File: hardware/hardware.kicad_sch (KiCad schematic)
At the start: 1 part, among them U1 ESP32-S3

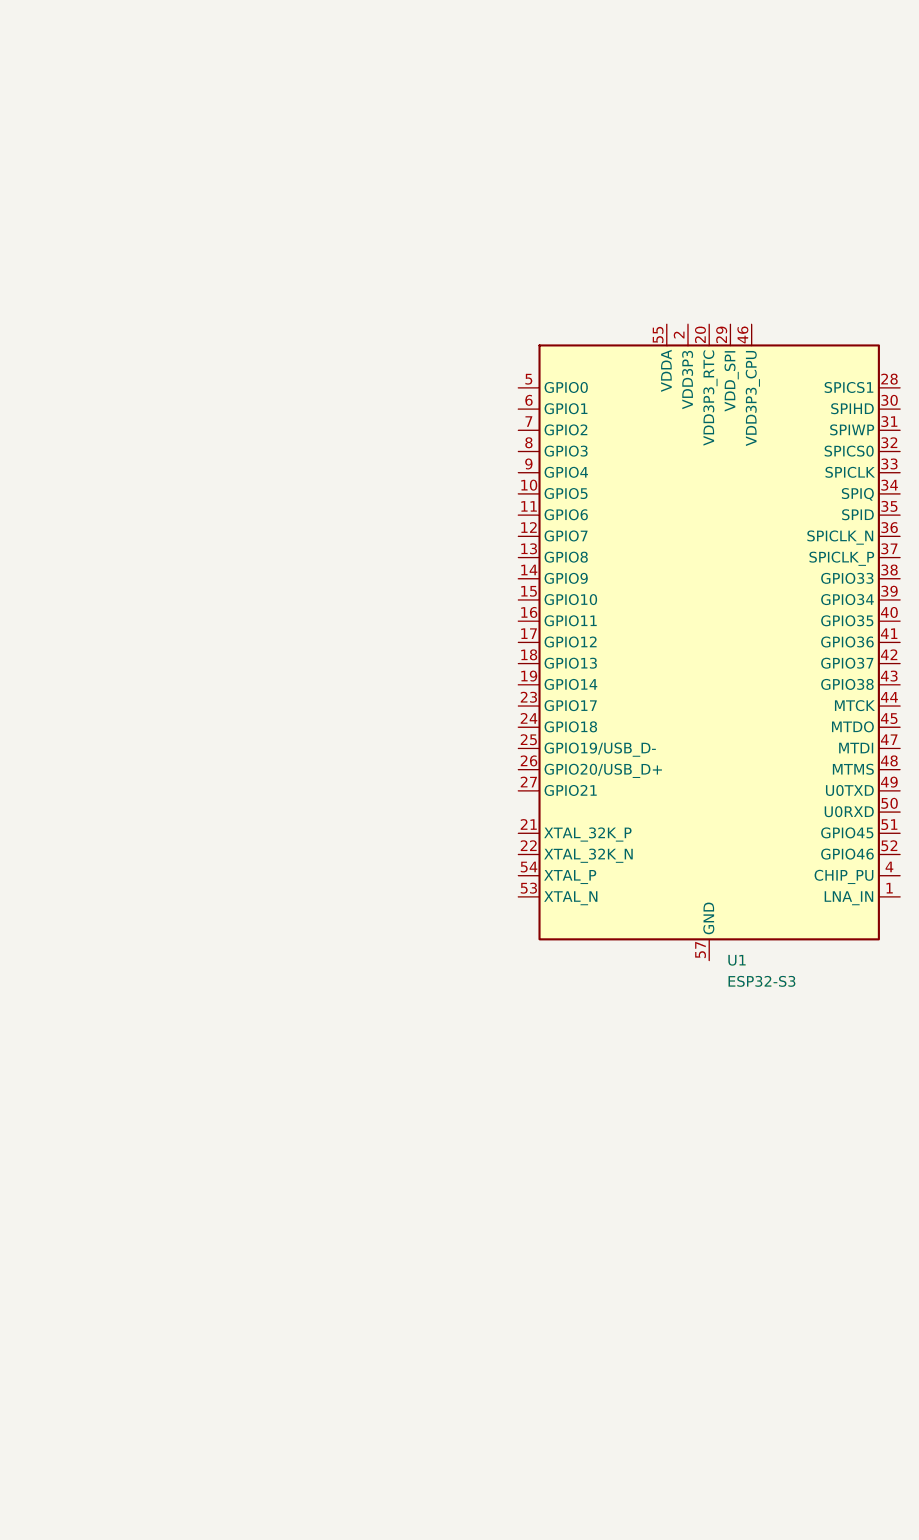
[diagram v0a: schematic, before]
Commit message: Adding usbc port
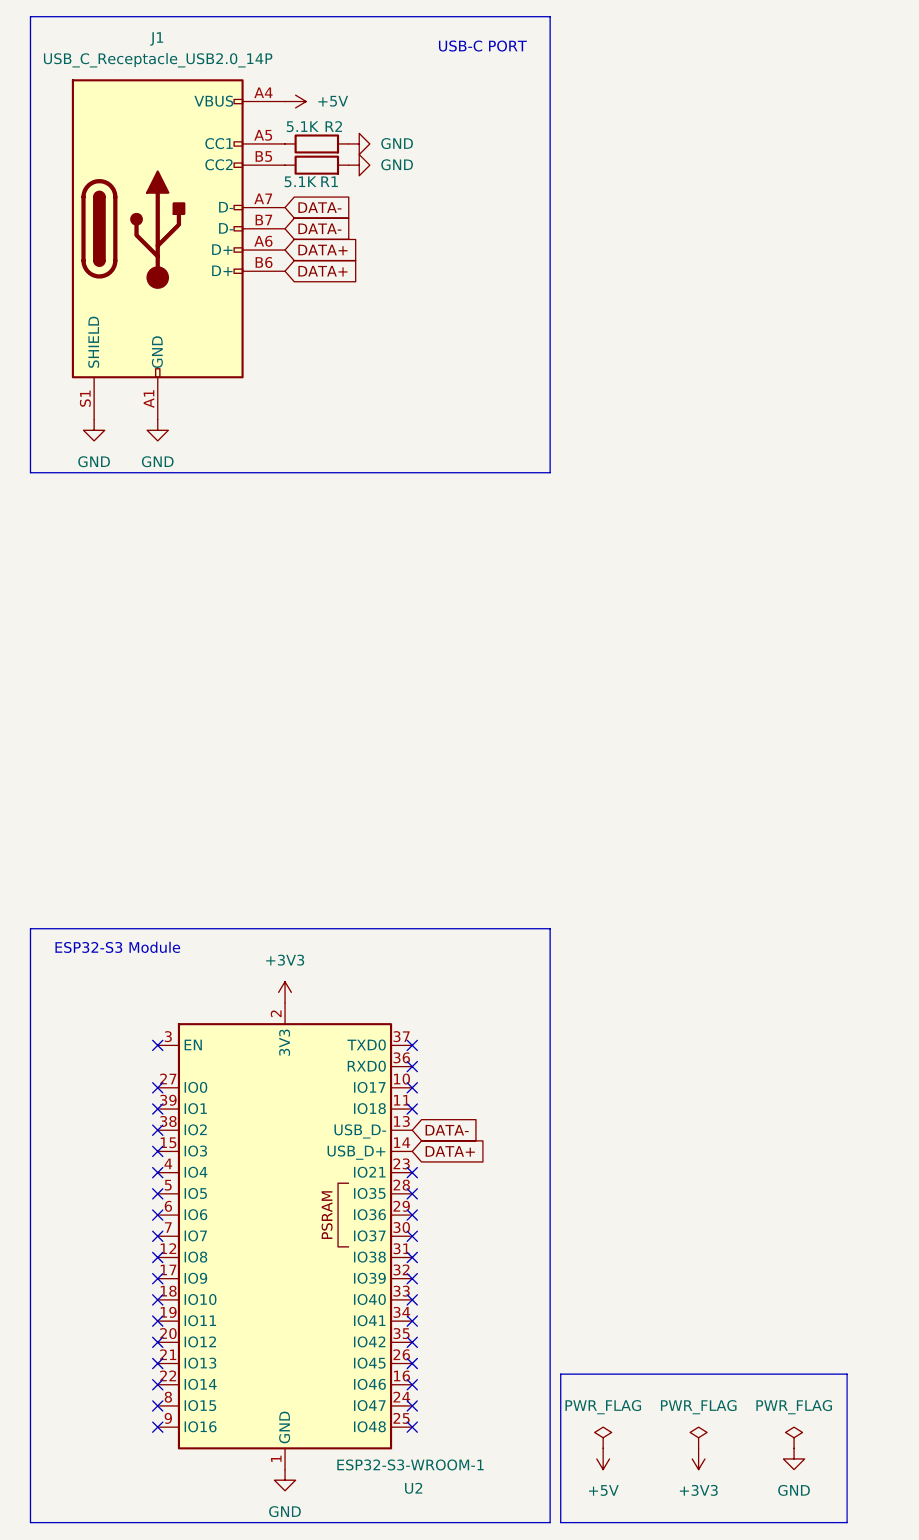
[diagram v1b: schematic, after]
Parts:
- removed U1: ESP32-S3, Package_DFN_QFN:QFN-56-1EP_7x7mm_P0.4mm_EP4x4mm, symbol MCU_Espressif:ESP32-S3
- added J1: USB_C_Receptacle_USB2.0_14P, symbol Connector:USB_C_Receptacle_USB2.0_14P
- added R1, R2: 5.1K, symbol Device:R
- added U2: ESP32-S3-WROOM-1, RF_Module:ESP32-S3-WROOM-1, symbol RF_Module:ESP32-S3-WROOM-1
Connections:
- new net: J1.A5 (CC1), R2.1
- new net: J1.B5 (CC2), R1.1
- new net +3V3: U2.2 (3V3)
- new net +5V: J1.A4 (VBUS), J1.A9 (VBUS), J1.B4 (VBUS), J1.B9 (VBUS)
- new net DATA+: J1.A6 (D+), J1.B6 (D+), U2.14 (USB_D+)
- new net DATA-: J1.A7 (D-), J1.B7 (D-), U2.13 (USB_D-)
- new net GND: J1.A1 (GND), J1.A12 (GND), J1.B1 (GND), J1.B12 (GND), J1.S1 (SHIELD), R1.2, R2.2, U2.1 (GND), U2.40 (GND), U2.41 (GND)
- no-connect marks 0 -> 35
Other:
- note added: "ESP32-S3 Module"
- note added: "USB-C PORT"
- company: (none) -> Trophées NSI
- title: (none) -> PlantMate

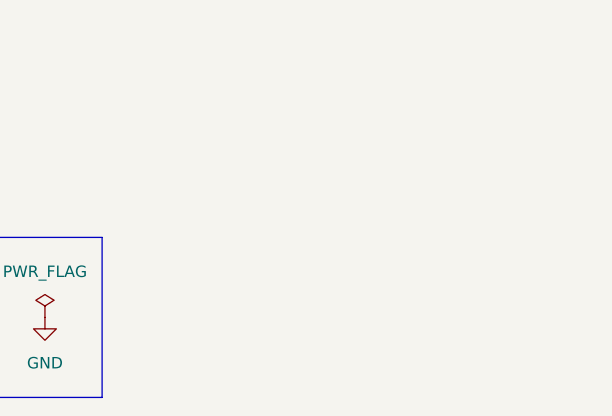
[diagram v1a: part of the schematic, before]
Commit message: Adding SPI pin socket
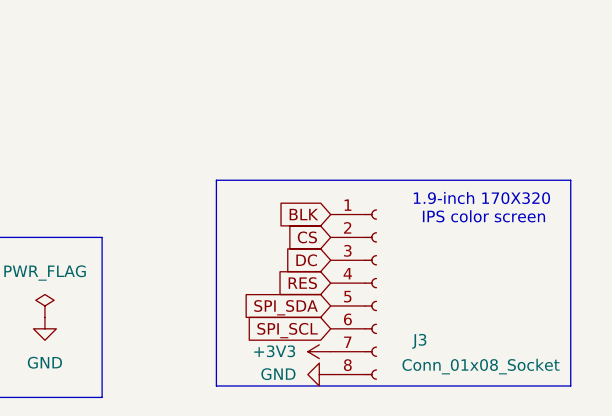
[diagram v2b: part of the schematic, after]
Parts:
- added J3: Conn_01x08_Socket, symbol Connector:Conn_01x08_Socket
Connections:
- net +3V3: now also J3.7 (Pin_7)
- net GND: now also J3.8 (Pin_8)
- new net BLK: J3.1 (Pin_1)
- new net CS: J3.2 (Pin_2)
- new net DC: J3.3 (Pin_3)
- new net RES: J3.4 (Pin_4)
- new net SPI_SCL: J3.6 (Pin_6)
- new net SPI_SDA: J3.5 (Pin_5)
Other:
- note added: "1.9-inch 170X320"
- note added: "IPS color screen"

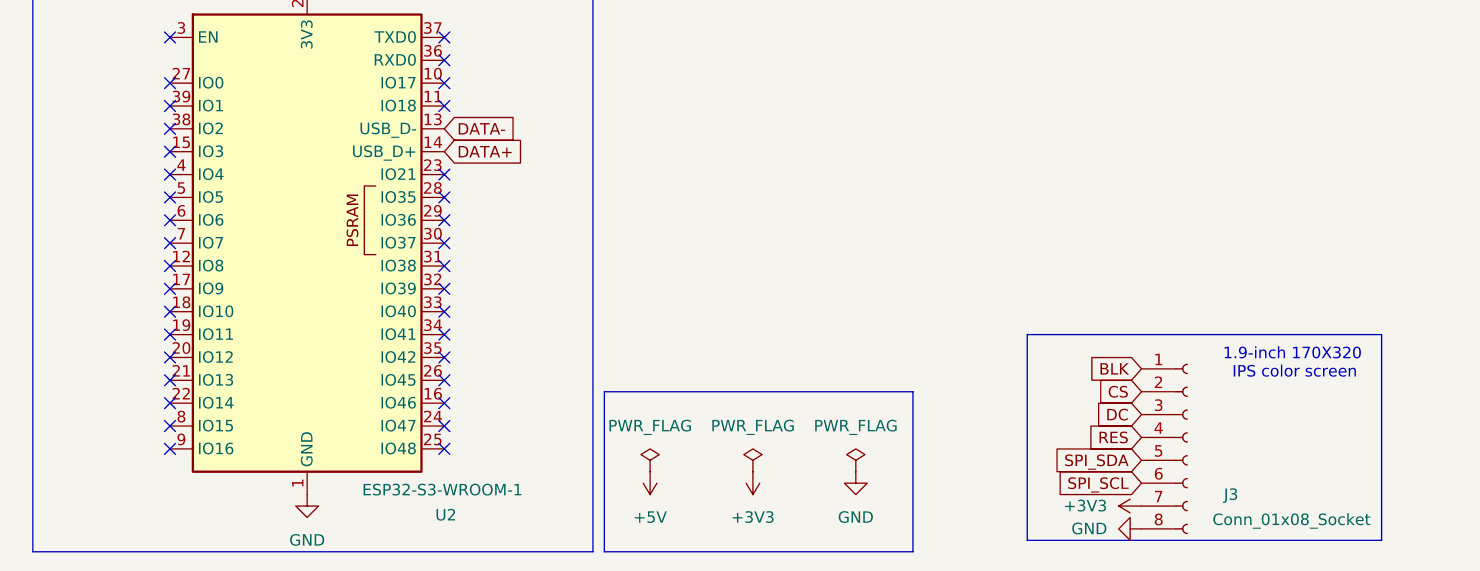
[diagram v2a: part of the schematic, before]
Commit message: [ERC GOOD] , correcting tag name MOSI & SCLk, Adding tags to ESP-32-S3
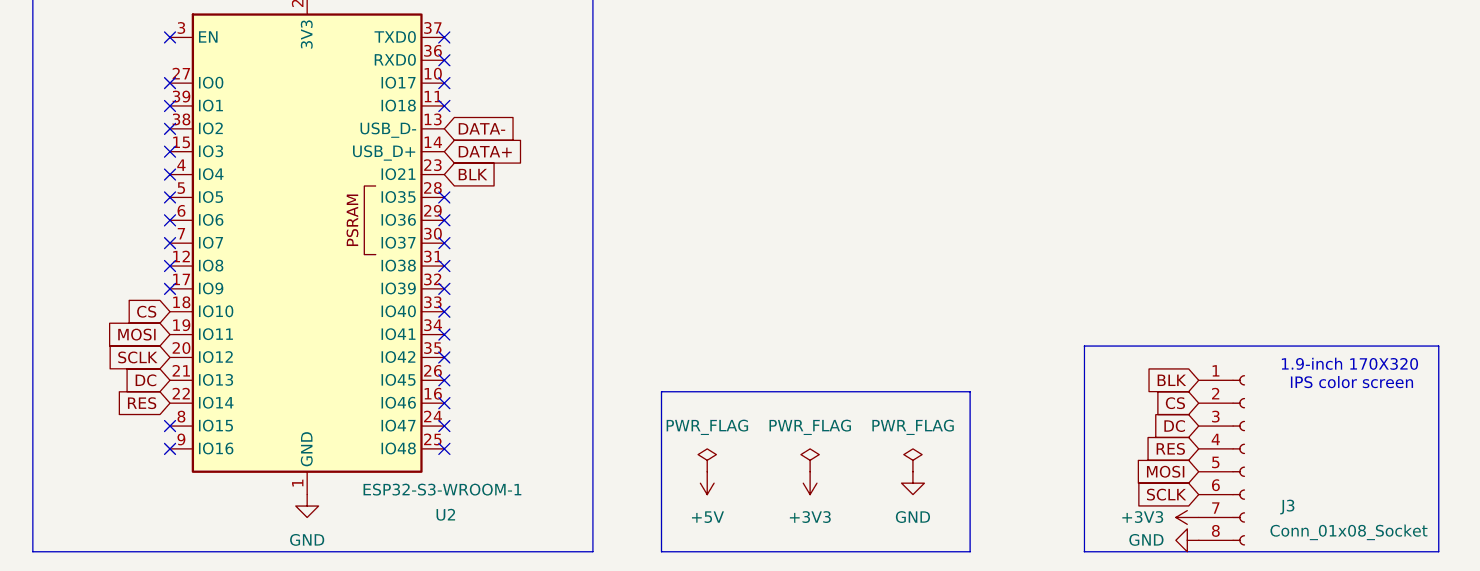
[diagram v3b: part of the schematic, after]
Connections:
- net SPI_SCL is gone; now on net SCLK: J3.6 (Pin_6)
- net SPI_SDA is gone; now on net MOSI: J3.5 (Pin_5)
- net BLK: now also U2.23 (IO21)
- net CS: now also U2.18 (IO10)
- net DC: now also U2.21 (IO13)
- net RES: now also U2.22 (IO14)
- net MOSI: now reaches U2.19 (IO11)
- net SCLK: now reaches U2.20 (IO12)
- no-connect marks 35 -> 29
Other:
- moved on the sheet: J3

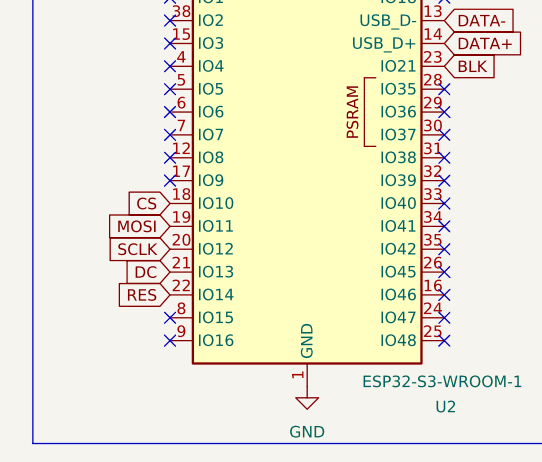
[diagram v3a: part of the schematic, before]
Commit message: Making PCB + screen route + switching CS and DC pins
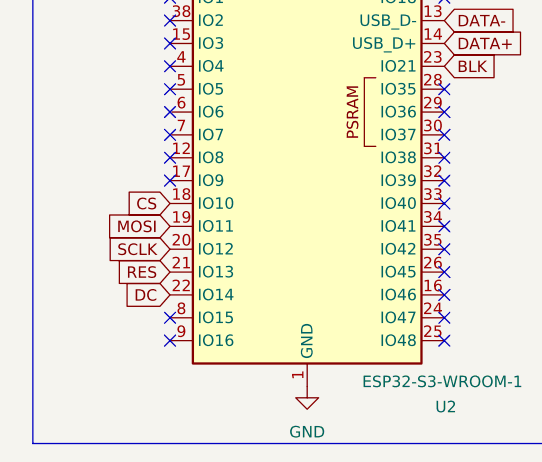
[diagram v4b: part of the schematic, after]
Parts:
- J1: footprint (none) -> Connector_USB:USB_C_Receptacle_HRO_TYPE-C-31-M-12
- J3: footprint (none) -> Connector_PinHeader_2.54mm:PinHeader_1x08_P2.54mm_Vertical
- R1, R2: footprint (none) -> Resistor_SMD:R_0805_2012Metric
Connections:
- net DC: now also U2.22 (IO14); no longer U2.21 (IO13)
- net RES: now also U2.21 (IO13); no longer U2.22 (IO14)
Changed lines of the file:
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@@
 		)
 	)
-	(global_label "DC"
+	(global_label "BLK"
 		(shape input)
-		(at 30.48 175.26 180)
+		(at 144.78 175.26 180)
 		(fields_autoplaced yes)
 		(effects
@@
 		)
 		(property "Intersheetrefs" "${INTERSHEET_REFS}"
-			(at 24.9548 175.26 0)
+			(at 138.2267 175.26 0)
 			(effects
 				(font
@@
 		)
 	)
-	(global_label "RES"
+	(global_label "BLK"
 		(shape input)
-		(at 30.48 177.8 180)
+		(at 60.96 152.4 0)
 		(fields_autoplaced yes)
 		(effects
@@
 				(size 1.27 1.27)
 			)
-			(justify right)
+			(justify left)
 		)
 		(property "Intersheetrefs" "${INTERSHEET_REFS}"
-			(at 23.8663 177.8 0)
-			(effects
-				(font
-					(size 1.27 1.27)
-				)
-				(justify right)
-				(hide yes)
-			)
-		)
-	)
-	(global_label "BLK"
+			(at 67.5133 152.4 0)
+			(effects
+				(font
+					(size 1.27 1.27)
+				)
+				(justify left)
+				(hide yes)
+			)
+		)
+	)
+	(global_label "DATA-"
 		(shape input)
-		(at 144.78 175.26 180)
+		(at 45.72 36.83 0)
 		(fields_autoplaced yes)
 		(effects
@@
 				(size 1.27 1.27)
 			)
-			(justify right)
+			(justify left)
 		)
 		(property "Intersheetrefs" "${INTERSHEET_REFS}"
-			(at 138.2267 175.26 0)
-			(effects
-				(font
-					(size 1.27 1.27)
-				)
-				(justify right)
-				(hide yes)
-			)
-		)
-	)
-	(global_label "BLK"
+			(at 54.6924 36.83 0)
+			(effects
+				(font
+					(size 1.27 1.27)
+				)
+				(justify left)
+				(hide yes)
+			)
+		)
+	)
+	(global_label "RES"
 		(shape input)
-		(at 60.96 152.4 0)
+		(at 30.48 175.26 180)
 		(fields_autoplaced yes)
 		(effects
@@
 				(size 1.27 1.27)
 			)
-			(justify left)
+			(justify right)
 		)
 		(property "Intersheetrefs" "${INTERSHEET_REFS}"
-			(at 67.5133 152.4 0)
-			(effects
-				(font
-					(size 1.27 1.27)
-				)
-				(justify left)
-				(hide yes)
-			)
-		)
-	)
-	(global_label "DATA-"
+			(at 23.8663 175.26 0)
+			(effects
+				(font
+					(size 1.27 1.27)
+				)
+				(justify right)
+				(hide yes)
+			)
+		)
+	)
+	(global_label "DC"
 		(shape input)
-		(at 45.72 36.83 0)
+		(at 30.48 177.8 180)
 		(fields_autoplaced yes)
 		(effects
@@
 				(size 1.27 1.27)
 			)
-			(justify left)
+			(justify right)
 		)
 		(property "Intersheetrefs" "${INTERSHEET_REFS}"
-			(at 54.6924 36.83 0)
-			(effects
-				(font
-					(size 1.27 1.27)
-				)
-				(justify left)
+			(at 24.9548 177.8 0)
+			(effects
+				(font
+					(size 1.27 1.27)
+				)
+				(justify right)
 				(hide yes)
 			)
@@
 			)
 		)
-		(property "Footprint" ""
+		(property "Footprint" "Connector_USB:USB_C_Receptacle_HRO_TYPE-C-31-M-12"
 			(at 34.29 39.37 0)
 			(effects
@@
 			)
 		)
-		(property "Footprint" ""
+		(property "Footprint" "Connector_PinHeader_2.54mm:PinHeader_1x08_P2.54mm_Vertical"
 			(at 149.86 182.88 0)
 			(effects
@@
 			)
 		)
-		(property "Footprint" ""
+		(property "Footprint" "Resistor_SMD:R_0805_2012Metric"
 			(at 49.53 33.528 90)
 			(effects
@@
 			)
 		)
-		(property "Footprint" ""
+		(property "Footprint" "Resistor_SMD:R_0805_2012Metric"
 			(at 49.53 30.988 90)
 			(effects
